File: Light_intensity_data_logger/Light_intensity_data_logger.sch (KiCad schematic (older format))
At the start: 23 parts, among them J1 Wire_to_Vbat, Q1 NTJD4001NT1G, Q2 NTJD4001NT1G, U1 BME280, U2 TCS34725FN, U3 TSL25911FN, U4 Teensy3.6

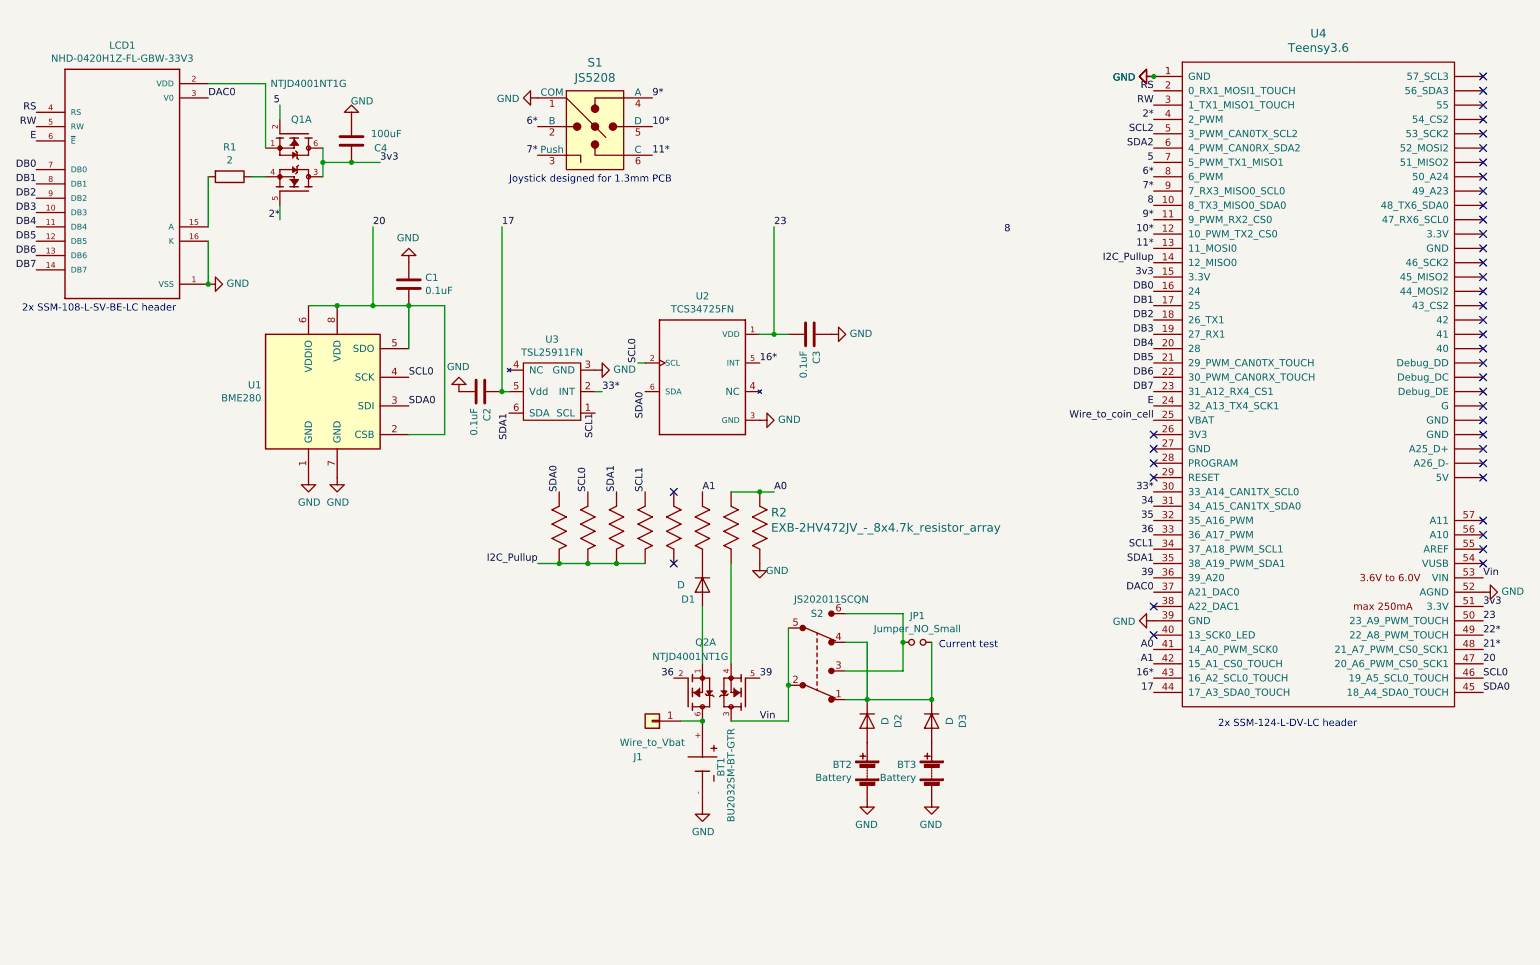
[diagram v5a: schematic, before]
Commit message: Complete routed draft - pass DRC other than courtyard
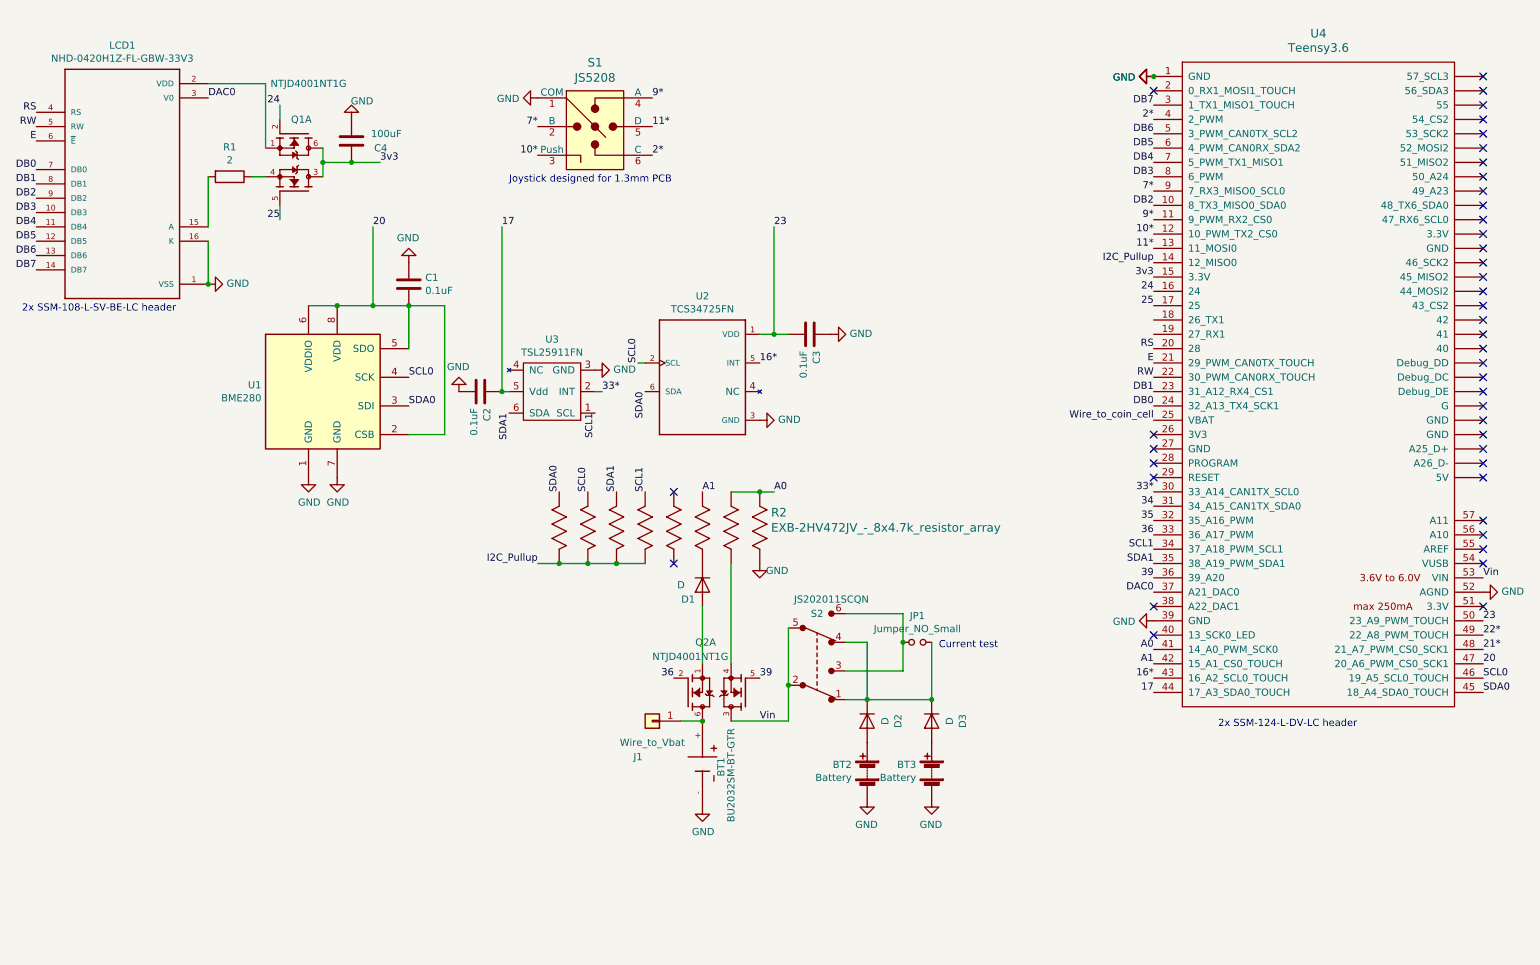
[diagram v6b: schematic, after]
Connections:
- net 8 is gone; now on net DB2: U4.10 (8_TX3_MISO0_SDA0)
- net SCL2 is gone; now on net DB6: U4.5 (3_PWM_CAN0TX_SCL2)
- net SDA2 is gone; now on net DB5: U4.6 (4_PWM_CAN0RX_SDA2)
- net 10*: now also S1.3 (Push); no longer S1.5 (D)
- net 11*: now also S1.5 (D); no longer S1.6 (C)
- net 2*: now also S1.6 (C); no longer Q1.5 (G2)
- net 3v3: no longer U4.51 (3.3V)
- net 7*: now also S1.2 (B); no longer S1.3 (Push)
- net DB0: now also U4.24 (32_A13_TX4_SCK1); no longer U4.16 (24)
- net DB1: now also U4.23 (31_A12_RX4_CS1); no longer U4.17 (25)
- net DB2: no longer U4.18 (26_TX1)
- net DB3: now also U4.8 (6_PWM); no longer U4.19 (27_RX1)
- net DB4: now also U4.7 (5_PWM_TX1_MISO1); no longer U4.20 (28)
- net DB5: no longer U4.21 (29_PWM_CAN0TX_TOUCH)
- net DB6: no longer U4.22 (30_PWM_CAN0RX_TOUCH)
- net DB7: now also U4.3 (1_TX1_MISO1_TOUCH); no longer U4.23 (31_A12_RX4_CS1)
- net E: now also U4.21 (29_PWM_CAN0TX_TOUCH); no longer U4.24 (32_A13_TX4_SCK1)
- net RS: now also U4.20 (28); no longer U4.2 (0_RX1_MOSI1_TOUCH)
- net RW: now also U4.22 (30_PWM_CAN0RX_TOUCH); no longer U4.3 (1_TX1_MISO1_TOUCH)
- net 5 renamed 24
- net 24: now also U4.16 (24); no longer U4.7 (5_PWM_TX1_MISO1)
- removed net 6*: S1.2 (B), U4.8 (6_PWM)
- new net 25: Q1.5 (G2), U4.17 (25)
- no-connect marks 41 -> 43
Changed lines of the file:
@@
 Text Label 10950 4350 0    50   ~ 0
 Vin
-Text Label 10950 4550 0    50   ~ 0
-3v3
 $Comp
 L power:GND #PWR0102
@@
 Text Label 10950 4850 0    50   ~ 0
 21*
-Text Label 2550 1850 2    50   ~ 0
-2*
-Text Label 2550 1050 2    50   ~ 0
-5
 $Comp
 L conn:Conn_01x01 J1
@@
 Text Label 8650 3250 2    50   ~ 0
 Wire_to_coin_cell
-Text Label 8650 1450 2    50   ~ 0
-5
 Text Label 6000 3750 0    50   ~ 0
 A0
@@
 Wire Wire Line
 	5900 2650 6000 2650
-Text Label 5150 1400 0    50   ~ 0
+Text Label 5150 1200 0    50   ~ 0
 11*
-Text Label 5150 1200 0    50   ~ 0
+Text Label 4350 1400 2    50   ~ 0
 10*
 Text Label 5150 1000 0    50   ~ 0
 9*
-Text Label 4350 1400 2    50   ~ 0
+Text Label 4350 1200 2    50   ~ 0
 7*
-Text Label 4350 1200 2    50   ~ 0
-6*
 $Comp
 L power:GND #PWR0111
@@
 $EndComp
 Connection ~ 8650 850
-Text Label 8650 1050 2    50   ~ 0
+Text Label 8650 2950 2    50   ~ 0
 RW
-Text Label 8650 950  2    50   ~ 0
+Text Label 8650 2750 2    50   ~ 0
 RS
 $Comp
@@
 Text Label 8650 2150 2    50   ~ 0
 I2C_Pullup
+Text Label 8650 2850 2    50   ~ 0
+E
+Text Label 8650 1050 2    50   ~ 0
+DB7
+Text Label 8650 1250 2    50   ~ 0
+DB6
+Text Label 8650 1350 2    50   ~ 0
+DB5
+Text Label 8650 1450 2    50   ~ 0
+DB4
+Text Label 8650 1550 2    50   ~ 0
+DB3
+Text Label 8650 1750 2    50   ~ 0
+DB2
+Text Label 8650 3050 2    50   ~ 0
+DB1
 Text Label 8650 3150 2    50   ~ 0
-E
-Text Label 8650 3050 2    50   ~ 0
-DB7
-Text Label 8650 2950 2    50   ~ 0
-DB6
-Text Label 8650 2850 2    50   ~ 0
-DB5
-Text Label 8650 2750 2    50   ~ 0
-DB4
-Text Label 8650 2650 2    50   ~ 0
-DB3
-Text Label 8650 2550 2    50   ~ 0
-DB2
-Text Label 8650 2450 2    50   ~ 0
-DB1
-Text Label 8650 2350 2    50   ~ 0
 DB0
 Text Label 8650 2050 2    50   ~ 0
@@
 NoConn ~ 8650 3650
 NoConn ~ 8650 3550
-Text Label 8650 1250 2    50   ~ 0
-SCL2
-Text Label 8650 1350 2    50   ~ 0
-SDA2
-Text Label 8650 1550 2    50   ~ 0
-6*
 Text Label 3450 3150 0    50   ~ 0
 SDA0
@@
 Text Label 5100 3750 1    50   ~ 0
 SCL1
-Text Label 8650 1750 2    50   ~ 0
-8
-Text Label 7650 1950 2    50   ~ 0
-8
 Text Label 5300 5050 2    50   ~ 0
 36
@@
 Wire Wire Line
 	5700 5350 6100 5350
+Text Label 8650 2350 2    50   ~ 0
+24
+Text Label 2550 1050 2    50   ~ 0
+24
+Text Label 8650 2450 2    50   ~ 0
+25
+Text Label 2550 1850 2    50   ~ 0
+25
+NoConn ~ 10950 4550
+Text Label 5150 1400 0    50   ~ 0
+2*
+NoConn ~ 8650 950
 $EndSCHEMATC

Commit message: License info and annotations added
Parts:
- renumbered C3 to C2, C2 to C3
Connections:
- net 21*: no longer names the net of U4.48 (21_A7_PWM_CS0_SCK1)
- net 22*: no longer names the net of U4.49 (22_A8_PWM_TOUCH)
- net 34: no longer names the net of U4.31 (34_A15_CAN1TX_SDA0)
- net 35: no longer names the net of U4.32 (35_A16_PWM)
- no-connect marks 43 -> 49
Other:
- moved on the sheet: C2, C3, U2, U3
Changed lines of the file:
@@
 L power:GND #PWR0106
 U 1 1 5E23FAAA
-P 3800 3050
-F 0 "#PWR0106" H 3800 2800 50  0001 C CNN
-F 1 "GND" H 3805 2877 50  0000 C CNN
-F 2 "" H 3800 3050 50  0001 C CNN
-F 3 "" H 3800 3050 50  0001 C CNN
-	1    3800 3050
-	-1   0    0    1
+P 5850 3050
+F 0 "#PWR0106" H 5850 2800 50  0001 C CNN
+F 1 "GND" V 5750 3000 50  0000 C CNN
+F 2 "" H 5850 3050 50  0001 C CNN
+F 3 "" H 5850 3050 50  0001 C CNN
+	1    5850 3050
+	0    1    1    0
 $EndComp
 Wire Wire Line
@@
 Text Label 850  1300 2    50   ~ 0
 E
-Text Label 10950 4750 0    50   ~ 0
-22*
 Text Label 4350 4250 2    50   ~ 0
 I2C_Pullup
@@
 Text Label 8650 5150 2    50   ~ 0
 17
-Text Label 5900 2850 0    50   ~ 0
+Text Label 4950 2950 0    50   ~ 0
 16*
-Text Label 4100 1900 0    50   ~ 0
+Text Label 6150 1900 0    50   ~ 0
 17
 $Comp
@@
 	0    -1   -1   0
 $EndComp
-Text Label 10950 4850 0    50   ~ 0
-21*
 $Comp
 L conn:Conn_01x01 J1
@@
 Text Label 8650 4050 2    50   ~ 0
 36
-Text Label 8650 3950 2    50   ~ 0
-35
-Text Label 8650 3850 2    50   ~ 0
-34
-Wire Wire Line
-	6000 2650 6100 2650
-Connection ~ 6000 2650
-Wire Wire Line
-	6000 2650 6000 1900
+Wire Wire Line
+	5050 2750 5150 2750
+Connection ~ 5050 2750
 Connection ~ 5900 3750
 Wire Wire Line
@@
 	6000 3750 5900 3750
 Wire Wire Line
-	5900 2650 6000 2650
+	4950 2750 5050 2750
 Text Label 5150 1200 0    50   ~ 0
 11*
@@
 NoConn ~ 5300 3750
 $Comp
+L device:C C2
+U 1 1 5E2CDF37
+P 5300 2750
+F 0 "C2" H 5415 2796 50  0000 L CNN
+F 1 "0.1uF" H 5415 2705 50  0000 L CNN
+F 2 "Capacitors_SMD:C_0603" H 5338 2600 50  0001 C CNN
+F 3 "https://media.digikey.com/pdf/Data%20Sheets/Samsunghttps://www.yageo.com/upload/media/product/productsearch/datasheet/mlcc/UPY-GPHC_X7R_6.3V-to-50V_18.pdf" H 5300 2750 50  0001 C CNN
+F 4 "311-1344-1-ND" H 5300 2750 50  0001 C CNN "Part#"
+	1    5300 2750
+	0    1    1    0
+$EndComp
+Connection ~ 6150 3050
+$Comp
 L device:C C3
-U 1 1 5E2CDF37
-P 6250 2650
-F 0 "C3" H 6365 2696 50  0000 L CNN
-F 1 "0.1uF" H 6365 2605 50  0000 L CNN
-F 2 "Capacitors_SMD:C_0603" H 6288 2500 50  0001 C CNN
-F 3 "https://media.digikey.com/pdf/Data%20Sheets/Samsunghttps://www.yageo.com/upload/media/product/productsearch/datasheet/mlcc/UPY-GPHC_X7R_6.3V-to-50V_18.pdf" H 6250 2650 50  0001 C CNN
-F 4 "311-1344-1-ND" H 6250 2650 50  0001 C CNN "Part#"
-	1    6250 2650
-	0    1    1    0
-$EndComp
-Connection ~ 4100 3050
-$Comp
-L device:C C2
 U 1 1 5E2CD370
-P 3950 3050
-F 0 "C2" H 4065 3096 50  0000 L CNN
-F 1 "0.1uF" H 4065 3005 50  0000 L CNN
-F 2 "Capacitors_SMD:C_0603" H 3988 2900 50  0001 C CNN
-F 3 "https://media.digikey.com/pdf/Data%20Sheets/Samsunghttps://www.yageo.com/upload/media/product/productsearch/datasheet/mlcc/UPY-GPHC_X7R_6.3V-to-50V_18.pdf" H 3950 3050 50  0001 C CNN
-F 4 "311-1344-1-ND" H 3950 3050 50  0001 C CNN "Part#"
-	1    3950 3050
-	0    1    1    0
-$EndComp
-Wire Wire Line
-	4100 1900 4100 3050
-Wire Wire Line
-	4150 3050 4100 3050
+P 6000 3050
+F 0 "C3" H 6115 3096 50  0000 L CNN
+F 1 "0.1uF" H 6115 3005 50  0000 L CNN
+F 2 "Capacitors_SMD:C_0603" H 6038 2900 50  0001 C CNN
+F 3 "https://media.digikey.com/pdf/Data%20Sheets/Samsunghttps://www.yageo.com/upload/media/product/productsearch/datasheet/mlcc/UPY-GPHC_X7R_6.3V-to-50V_18.pdf" H 6000 3050 50  0001 C CNN
+F 4 "311-1344-1-ND" H 6000 3050 50  0001 C CNN "Part#"
+	1    6000 3050
+	0    1    1    0
+$EndComp
+Wire Wire Line
+	6150 1900 6150 3050
+Wire Wire Line
+	6200 3050 6150 3050
 $Comp
 L power:GND #PWR0113
 U 1 1 5E241861
-P 6400 2650
-F 0 "#PWR0113" H 6400 2400 50  0001 C CNN
-F 1 "GND" V 6405 2522 50  0000 R CNN
-F 2 "" H 6400 2650 50  0001 C CNN
-F 3 "" H 6400 2650 50  0001 C CNN
-	1    6400 2650
+P 5450 2750
+F 0 "#PWR0113" H 5450 2500 50  0001 C CNN
+F 1 "GND" V 5455 2622 50  0000 R CNN
+F 2 "" H 5450 2750 50  0001 C CNN
+F 3 "" H 5450 2750 50  0001 C CNN
+	1    5450 2750
 	0    -1   -1   0
 $EndComp
@@
 NoConn ~ 8650 3650
 NoConn ~ 8650 3550
-Text Label 3450 3150 0    50   ~ 0
-SDA0
-Text Label 5050 2850 1    50   ~ 0
+Text Label 3950 2950 2    50   ~ 0
 SCL0
 Text Label 8650 4150 2    50   ~ 0
@@
 L power:GND #PWR0114
 U 1 1 5E2152EA
-P 4750 2900
-F 0 "#PWR0114" H 4750 2650 50  0001 C CNN
-F 1 "GND" V 4755 2772 50  0000 R CNN
-F 2 "" H 4750 2900 50  0001 C CNN
-F 3 "" H 4750 2900 50  0001 C CNN
-	1    4750 2900
+P 6800 2900
+F 0 "#PWR0114" H 6800 2650 50  0001 C CNN
+F 1 "GND" V 6805 2772 50  0000 R CNN
+F 2 "" H 6800 2900 50  0001 C CNN
+F 3 "" H 6800 2900 50  0001 C CNN
+	1    6800 2900
 	0    -1   -1   0
 $EndComp
@@
 2*
 Wire Wire Line
-	4750 3050 4800 3050
-Wire Wire Line
-	5100 2850 5050 2850
+	6800 3050 6850 3050
 $Comp
 L power:GND #PWR0115
 U 1 1 5E1FF1C2
-P 5900 3250
-F 0 "#PWR0115" H 5900 3000 50  0001 C CNN
-F 1 "GND" V 5905 3122 50  0000 R CNN
-F 2 "" H 5900 3250 50  0001 C CNN
-F 3 "" H 5900 3250 50  0001 C CNN
-	1    5900 3250
+P 4950 3350
+F 0 "#PWR0115" H 4950 3100 50  0001 C CNN
+F 1 "GND" V 4955 3222 50  0000 R CNN
+F 2 "" H 4950 3350 50  0001 C CNN
+F 3 "" H 4950 3350 50  0001 C CNN
+	1    4950 3350
 	0    -1   -1   0
 $EndComp
@@
 L Ben_custom:TSL25911FN U3
 U 1 1 5E1E6521
-P 4450 3050
-F 0 "U3" H 4450 2685 50  0000 C CNN
-F 1 "TSL25911FN" H 4450 2776 50  0000 C CNN
-F 2 "Ben_Custom:TSL25911FN" H 4050 3500 50  0001 C CNN
-F 3 "https://ams.com/documents/20143/36005/TSL2591_DS000338_6-00.pdf" H 4050 3500 50  0001 C CNN
-F 4 "TSL25911FNCT-ND" H 4450 3050 50  0001 C CNN "Part#"
-	1    4450 3050
+P 6500 3050
+F 0 "U3" H 6500 2685 50  0000 C CNN
+F 1 "TSL25911FN" H 6500 2776 50  0000 C CNN
+F 2 "Ben_Custom:TSL25911FN" H 6100 3500 50  0001 C CNN
+F 3 "https://ams.com/documents/20143/36005/TSL2591_DS000338_6-00.pdf" H 6100 3500 50  0001 C CNN
+F 4 "TSL25911FNCT-ND" H 6500 3050 50  0001 C CNN "Part#"
+	1    6500 3050
 	-1   0    0    1
 $EndComp
@@
 L Ben_custom:TCS34725FN U2
 U 1 1 5E1E525D
-P 5500 2950
-F 0 "U2" H 5500 3517 50  0000 C CNN
-F 1 "TCS34725FN" H 5500 3426 50  0000 C CNN
-F 2 "Ben_Custom:TCS34725" H 5150 3450 50  0001 L BNN
-F 3 "https://ams.com/documents/20143/36005/TCS3472_DS000390_2-00.pdf" H 5150 2450 50  0001 L BNN
-F 4 "TCS34725FNCT-ND" H 5500 2950 50  0001 C CNN "Part#"
-	1    5500 2950
+P 4550 3050
+F 0 "U2" H 4550 3617 50  0000 C CNN
+F 1 "TCS34725FN" H 4550 3526 50  0000 C CNN
+F 2 "Ben_Custom:TCS34725" H 4200 3550 50  0001 L BNN
+F 3 "https://ams.com/documents/20143/36005/TCS3472_DS000390_2-00.pdf" H 4200 2550 50  0001 L BNN
+F 4 "TCS34725FNCT-ND" H 4550 3050 50  0001 C CNN "Part#"
+	1    4550 3050
 	1    0    0    -1
 $EndComp
@@
 Text Label 10950 5150 0    50   ~ 0
 SDA0
-Text Label 4750 3200 3    50   ~ 0
+Text Label 6800 3200 3    50   ~ 0
 SCL1
-Text Label 4150 3200 3    50   ~ 0
+Text Label 6200 3200 3    50   ~ 0
 SDA1
 Wire Wire Line
@@
 	0    -1   1    0
 $EndComp
-Text Label 3450 2950 0    50   ~ 0
-SCL0
-Text Label 5100 3050 3    50   ~ 0
+Text Label 3950 3150 2    50   ~ 0
 SDA0
 Text Label 10950 4950 0    50   ~ 0
@@
 Text Label 10950 4650 0    50   ~ 0
 23
-Text Label 6000 1900 0    50   ~ 0
+Text Label 5050 1900 0    50   ~ 0
 23
 Text Label 8650 3750 2    50   ~ 0
 33*
-Text Label 4800 3050 0    50   ~ 0
+Text Label 6850 3050 0    50   ~ 0
 33*
 Text Label 4500 3750 1    50   ~ 0
@@
 2*
 NoConn ~ 8650 950
+NoConn ~ 8650 2550
+NoConn ~ 8650 2650
+NoConn ~ 8650 3850
+NoConn ~ 8650 3950
+NoConn ~ 10950 4850
+NoConn ~ 10950 4750
+Wire Wire Line
+	5050 1900 5050 2750
+Wire Wire Line
+	4150 2950 3450 2950
+Wire Wire Line
+	4150 3150 3450 3150
 $EndSCHEMATC

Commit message: Parts numbered in order, courtyards fixed, bigger banana pads
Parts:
- renumbered D2 to D1, D3 to D2, D1 to D3, R2 to R1, R1 to R2
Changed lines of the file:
@@
 	2050 1550 2050 1900
 $Comp
-L device:R R1
+L device:R R2
 U 1 1 5E2EF264
 P 2200 1550
-F 0 "R1" V 1993 1550 50  0000 C CNN
+F 0 "R2" V 1993 1550 50  0000 C CNN
 F 1 "2" V 2084 1550 50  0000 C CNN
 F 2 "Resistors_SMD:R_0603" V 2130 1550 50  0001 C CNN
@@
 $EndComp
 $Comp
-L device:D D2
+L device:D D1
 U 1 1 5E1F5931
 P 6650 5350
-F 0 "D2" H 6650 5134 50  0000 C CNN
+F 0 "D1" H 6650 5134 50  0000 C CNN
 F 1 "D" H 6650 5225 50  0000 C CNN
 F 2 "Diodes_SMD:D_SOD-323" H 6650 5350 50  0001 C CNN
@@
 	5700 3750 5900 3750
 $Comp
-L Ben_custom:EXB-2HV103JV_-_8x10k_resistor_array R2
+L Ben_custom:EXB-2HV103JV_-_8x10k_resistor_array R1
 U 1 1 5E2CE816
 P 5900 3750
-F 0 "R2" V 6044 3829 60  0000 L CNN
+F 0 "R1" V 6044 3829 60  0000 L CNN
 F 1 "EXB-2HV472JV_-_8x4.7k_resistor_array" V 6150 3829 60  0000 L CNN
 F 2 "Ben_Custom:Resistor_array_1506_8x" H 6150 3415 60  0001 C CNN
@@
 	6650 5200 7100 5200
 $Comp
-L device:D D3
+L device:D D2
 U 1 1 5E274B07
 P 7100 5350
-F 0 "D3" H 7100 5134 50  0000 C CNN
+F 0 "D2" H 7100 5134 50  0000 C CNN
 F 1 "D" H 7100 5225 50  0000 C CNN
 F 2 "Diodes_SMD:D_SOD-323" H 7100 5350 50  0001 C CNN
@@
 $EndComp
 $Comp
-L device:D D1
+L device:D D3
 U 1 1 5E2E8394
 P 5500 4400
-F 0 "D1" V 5600 4500 50  0000 C CNN
+F 0 "D3" V 5600 4500 50  0000 C CNN
 F 1 "D" V 5500 4550 50  0000 C CNN
 F 2 "Diodes_SMD:D_SOD-323" H 5500 4400 50  0001 C CNN
